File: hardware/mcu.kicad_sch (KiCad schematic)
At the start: 18 parts

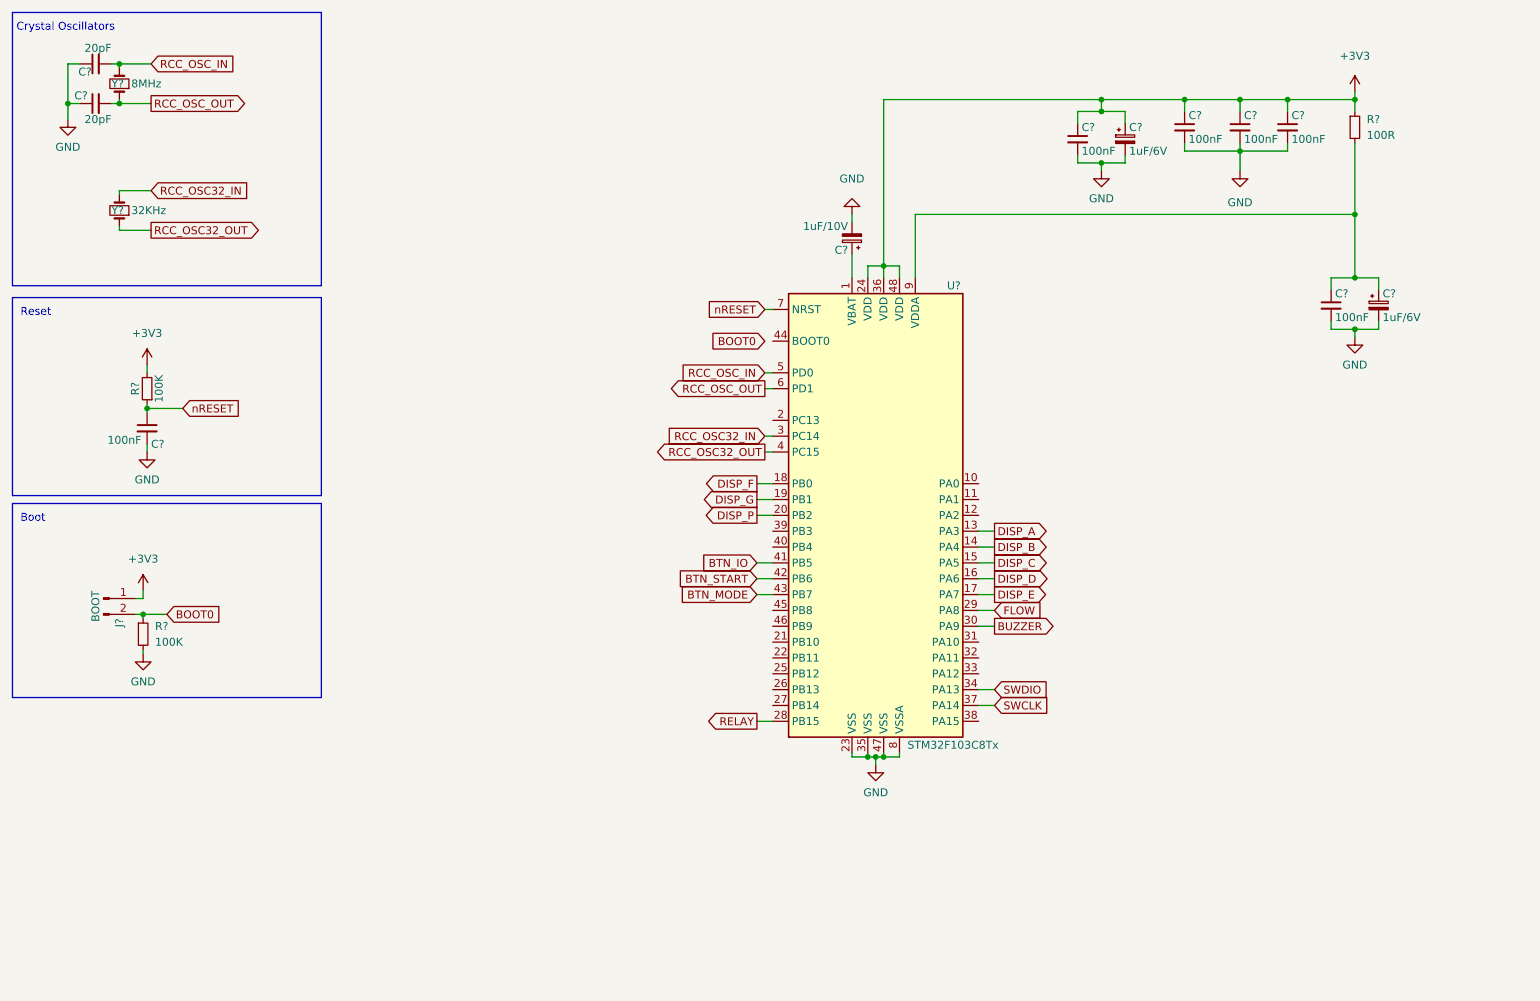
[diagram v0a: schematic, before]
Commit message: Display circuit added
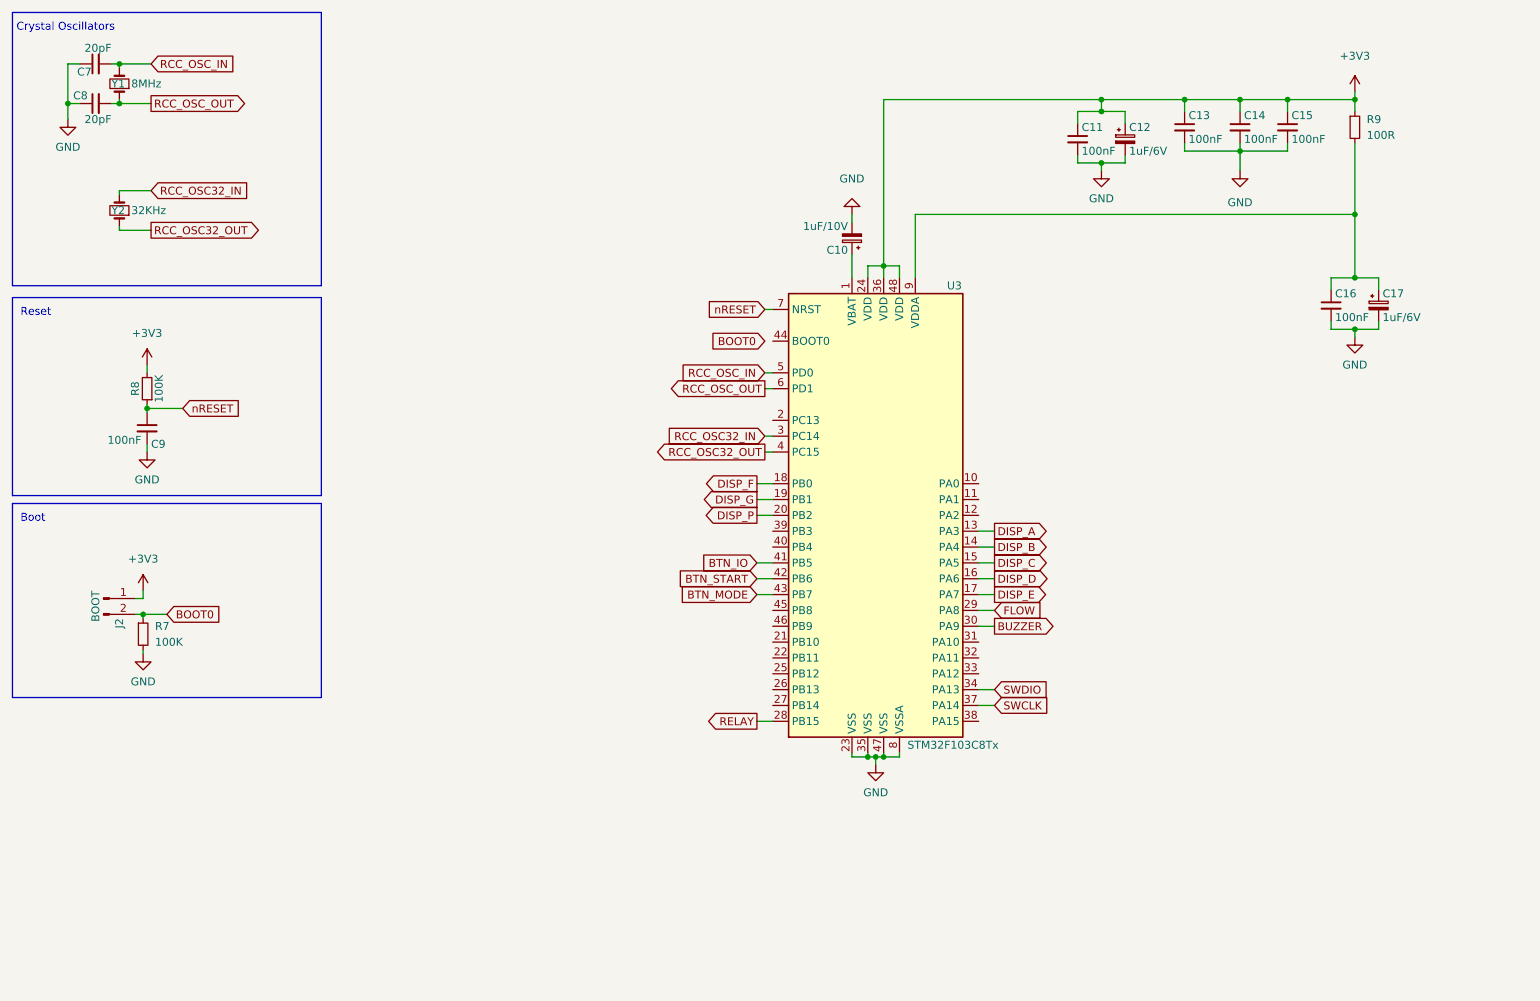
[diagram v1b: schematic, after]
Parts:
- gave numbers to parts that had none: 18
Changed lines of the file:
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@@
   (symbol (lib_id "power:GND") (at 188.595 38.735 0) (unit 1)
     (in_bom yes) (on_board yes) (fields_autoplaced)
-    (property "Reference" "#PWR?" (id 0) (at 188.595 45.085 0)
+    (property "Reference" "#PWR08" (id 0) (at 188.595 45.085 0)
       (effects (font (size 1.27 1.27)) hide)
     )
@@
   (symbol (lib_id "Device:Crystal_Small") (at 31.115 45.085 90) (unit 1)
     (in_bom yes) (on_board yes)
-    (property "Reference" "Y?" (id 0) (at 29.845 45.085 90)
+    (property "Reference" "Y2" (id 0) (at 29.845 45.085 90)
       (effects (font (size 1.27 1.27)) (justify right))
     )
@@
   (symbol (lib_id "Device:C_Small") (at 210.82 31.75 0) (unit 1)
     (in_bom yes) (on_board yes)
-    (property "Reference" "C?" (id 0) (at 211.455 29.845 0)
+    (property "Reference" "C14" (id 0) (at 211.455 29.845 0)
       (effects (font (size 1.27 1.27)) (justify left))
     )
@@
   (symbol (lib_id "power:+3V3") (at 35.56 69.85 0) (unit 1)
     (in_bom yes) (on_board yes) (fields_autoplaced)
-    (property "Reference" "#PWR?" (id 0) (at 35.56 73.66 0)
+    (property "Reference" "#PWR04" (id 0) (at 35.56 73.66 0)
       (effects (font (size 1.27 1.27)) hide)
     )
@@
   (symbol (lib_id "Device:R_Small") (at 35.56 73.66 180) (unit 1)
     (in_bom yes) (on_board yes)
-    (property "Reference" "R?" (id 0) (at 33.655 73.66 90))
+    (property "Reference" "R8" (id 0) (at 33.655 73.66 90))
     (property "Value" "100K" (id 1) (at 37.465 73.66 90))
     (property "Footprint" "" (id 2) (at 35.56 73.66 0)
@@
   (symbol (lib_id "Device:C_Polarized_Small") (at 148.59 49.53 180) (unit 1)
     (in_bom yes) (on_board yes)
-    (property "Reference" "C?" (id 0) (at 147.955 51.435 0)
+    (property "Reference" "C10" (id 0) (at 147.955 51.435 0)
       (effects (font (size 1.27 1.27)) (justify left))
     )
@@
   (symbol (lib_id "power:GND") (at 148.59 45.72 180) (unit 1)
     (in_bom yes) (on_board yes) (fields_autoplaced)
-    (property "Reference" "#PWR?" (id 0) (at 148.59 39.37 0)
+    (property "Reference" "#PWR06" (id 0) (at 148.59 39.37 0)
       (effects (font (size 1.27 1.27)) hide)
     )
@@
   (symbol (lib_id "Device:C_Polarized_Small") (at 192.405 33.655 0) (unit 1)
     (in_bom yes) (on_board yes)
-    (property "Reference" "C?" (id 0) (at 193.04 31.75 0)
+    (property "Reference" "C12" (id 0) (at 193.04 31.75 0)
       (effects (font (size 1.27 1.27)) (justify left))
     )
@@
   (symbol (lib_id "Device:C_Small") (at 184.785 33.655 0) (unit 1)
     (in_bom yes) (on_board yes)
-    (property "Reference" "C?" (id 0) (at 185.42 31.75 0)
+    (property "Reference" "C11" (id 0) (at 185.42 31.75 0)
       (effects (font (size 1.27 1.27)) (justify left))
     )
@@
   (symbol (lib_id "power:+3V3") (at 229.235 26.035 0) (unit 1)
     (in_bom yes) (on_board yes) (fields_autoplaced)
-    (property "Reference" "#PWR?" (id 0) (at 229.235 29.845 0)
+    (property "Reference" "#PWR010" (id 0) (at 229.235 29.845 0)
       (effects (font (size 1.27 1.27)) hide)
     )
@@
   (symbol (lib_id "power:GND") (at 35.56 83.82 0) (unit 1)
     (in_bom yes) (on_board yes) (fields_autoplaced)
-    (property "Reference" "#PWR?" (id 0) (at 35.56 90.17 0)
+    (property "Reference" "#PWR05" (id 0) (at 35.56 90.17 0)
       (effects (font (size 1.27 1.27)) hide)
     )
@@
   (symbol (lib_id "power:GND") (at 229.235 65.405 0) (unit 1)
     (in_bom yes) (on_board yes) (fields_autoplaced)
-    (property "Reference" "#PWR?" (id 0) (at 229.235 71.755 0)
+    (property "Reference" "#PWR019" (id 0) (at 229.235 71.755 0)
       (effects (font (size 1.27 1.27)) hide)
     )
@@
   (symbol (lib_id "Device:R_Small") (at 34.925 113.03 0) (unit 1)
     (in_bom yes) (on_board yes) (fields_autoplaced)
-    (property "Reference" "R?" (id 0) (at 36.83 111.7599 0)
+    (property "Reference" "R7" (id 0) (at 36.83 111.7599 0)
       (effects (font (size 1.27 1.27)) (justify left))
     )
@@
   (symbol (lib_id "Device:R_Small") (at 229.235 31.75 0) (unit 1)
     (in_bom yes) (on_board yes) (fields_autoplaced)
-    (property "Reference" "R?" (id 0) (at 231.14 30.4799 0)
+    (property "Reference" "R9" (id 0) (at 231.14 30.4799 0)
       (effects (font (size 1.27 1.27)) (justify left))
     )
@@
   (symbol (lib_id "Device:C_Small") (at 27.305 21.59 90) (unit 1)
     (in_bom yes) (on_board yes)
-    (property "Reference" "C?" (id 0) (at 26.67 22.86 90)
+    (property "Reference" "C7" (id 0) (at 26.67 22.86 90)
       (effects (font (size 1.27 1.27)) (justify left))
     )
@@
   (symbol (lib_id "Device:C_Small") (at 201.93 31.75 0) (unit 1)
     (in_bom yes) (on_board yes)
-    (property "Reference" "C?" (id 0) (at 202.565 29.845 0)
+    (property "Reference" "C13" (id 0) (at 202.565 29.845 0)
       (effects (font (size 1.27 1.27)) (justify left))
     )
@@
   (symbol (lib_id "Device:C_Polarized_Small") (at 233.045 60.325 0) (unit 1)
     (in_bom yes) (on_board yes)
-    (property "Reference" "C?" (id 0) (at 233.68 58.42 0)
+    (property "Reference" "C17" (id 0) (at 233.68 58.42 0)
       (effects (font (size 1.27 1.27)) (justify left))
     )
@@
   (symbol (lib_id "power:GND") (at 152.4 133.985 0) (unit 1)
     (in_bom yes) (on_board yes) (fields_autoplaced)
-    (property "Reference" "#PWR?" (id 0) (at 152.4 140.335 0)
+    (property "Reference" "#PWR07" (id 0) (at 152.4 140.335 0)
       (effects (font (size 1.27 1.27)) hide)
     )
@@
   (symbol (lib_id "Device:C_Small") (at 225.425 60.325 0) (unit 1)
     (in_bom yes) (on_board yes)
-    (property "Reference" "C?" (id 0) (at 226.06 58.42 0)
+    (property "Reference" "C16" (id 0) (at 226.06 58.42 0)
       (effects (font (size 1.27 1.27)) (justify left))
     )
@@
   (symbol (lib_id "Device:C_Small") (at 27.305 27.94 90) (unit 1)
     (in_bom yes) (on_board yes)
-    (property "Reference" "C?" (id 0) (at 26.035 26.67 90)
+    (property "Reference" "C8" (id 0) (at 26.035 26.67 90)
       (effects (font (size 1.27 1.27)) (justify left))
     )
@@
   (symbol (lib_id "Device:C_Small") (at 218.44 31.75 0) (unit 1)
     (in_bom yes) (on_board yes)
-    (property "Reference" "C?" (id 0) (at 219.075 29.845 0)
+    (property "Reference" "C15" (id 0) (at 219.075 29.845 0)
       (effects (font (size 1.27 1.27)) (justify left))
     )
@@
   (symbol (lib_id "power:GND") (at 22.86 30.48 0) (unit 1)
     (in_bom yes) (on_board yes) (fields_autoplaced)
-    (property "Reference" "#PWR?" (id 0) (at 22.86 36.83 0)
+    (property "Reference" "#PWR01" (id 0) (at 22.86 36.83 0)
       (effects (font (size 1.27 1.27)) hide)
     )
@@
   (symbol (lib_id "Connector:Conn_01x02_Male") (at 28.575 107.315 0) (unit 1)
     (in_bom yes) (on_board yes)
-    (property "Reference" "J?" (id 0) (at 31.115 110.49 90)
+    (property "Reference" "J2" (id 0) (at 31.115 110.49 90)
       (effects (font (size 1.27 1.27)) (justify right))
     )
@@
   (symbol (lib_id "power:GND") (at 34.925 116.205 0) (unit 1)
     (in_bom yes) (on_board yes) (fields_autoplaced)
-    (property "Reference" "#PWR?" (id 0) (at 34.925 122.555 0)
+    (property "Reference" "#PWR03" (id 0) (at 34.925 122.555 0)
       (effects (font (size 1.27 1.27)) hide)
     )
@@
   (symbol (lib_id "Device:C_Small") (at 35.56 80.01 0) (unit 1)
     (in_bom yes) (on_board yes)
-    (property "Reference" "C?" (id 0) (at 36.195 82.55 0)
+    (property "Reference" "C9" (id 0) (at 36.195 82.55 0)
       (effects (font (size 1.27 1.27)) (justify left))
     )
@@
   (symbol (lib_id "Device:Crystal_Small") (at 31.115 24.765 90) (unit 1)
     (in_bom yes) (on_board yes)
-    (property "Reference" "Y?" (id 0) (at 29.845 24.765 90)
+    (property "Reference" "Y1" (id 0) (at 29.845 24.765 90)
       (effects (font (size 1.27 1.27)) (justify right))
     )
@@
   (symbol (lib_id "power:GND") (at 210.82 38.735 0) (unit 1)
     (in_bom yes) (on_board yes) (fields_autoplaced)
-    (property "Reference" "#PWR?" (id 0) (at 210.82 45.085 0)
+    (property "Reference" "#PWR09" (id 0) (at 210.82 45.085 0)
       (effects (font (size 1.27 1.27)) hide)
     )
@@
   (symbol (lib_id "power:+3V3") (at 34.925 106.045 0) (unit 1)
     (in_bom yes) (on_board yes) (fields_autoplaced)
-    (property "Reference" "#PWR?" (id 0) (at 34.925 109.855 0)
+    (property "Reference" "#PWR02" (id 0) (at 34.925 109.855 0)
       (effects (font (size 1.27 1.27)) hide)
     )
@@
   (symbol (lib_id "MCU_ST_STM32F1:STM32F103C8Tx") (at 153.67 93.98 0) (unit 1)
     (in_bom yes) (on_board yes)
-    (property "Reference" "U?" (id 0) (at 163.83 57.15 0)
-      (effects (font (size 1.27 1.27)) (justify left))
-    )
+    (property "Reference" "U3" (id 0) (at 163.83 57.15 0)
+      (effects (font (size 1.27 1.27)) (justify left))
+    )

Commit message: Schematics are completed
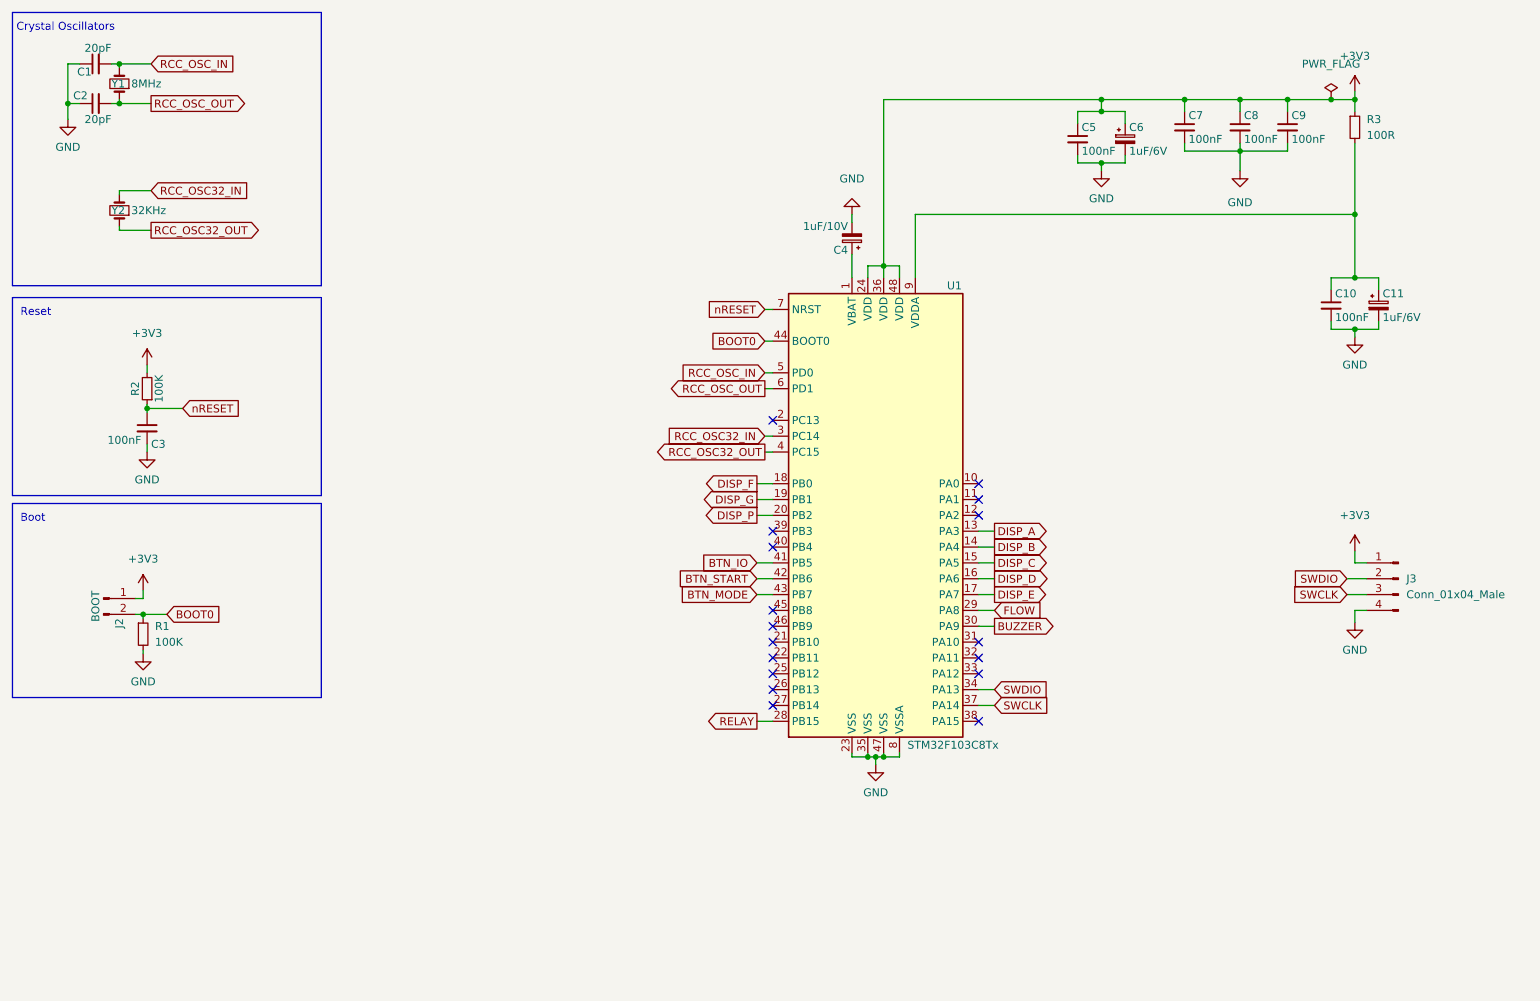
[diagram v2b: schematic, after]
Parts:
- added J3: Conn_01x04_Male, Connector_PinHeader_2.54mm:PinHeader_1x04_P2.54mm_Vertical, symbol Connector:Conn_01x04_Male
- C1: renamed from C7; footprint (none) -> Capacitor_SMD:C_0603_1608Metric
- C10: renamed from C16; footprint (none) -> Capacitor_SMD:C_0603_1608Metric
- C11: renamed from C17; footprint (none) -> Capacitor_SMD:CP_Elec_6.3x7.7
- C2: renamed from C8; footprint (none) -> Capacitor_SMD:C_0603_1608Metric
- C3: renamed from C9; footprint (none) -> Capacitor_SMD:C_0603_1608Metric
- C4: renamed from C10; footprint (none) -> Capacitor_SMD:CP_Elec_6.3x7.7
- C5: renamed from C11; footprint (none) -> Capacitor_SMD:C_0603_1608Metric
- C6: renamed from C12; footprint (none) -> Capacitor_SMD:CP_Elec_6.3x7.7
- C7: renamed from C13; footprint (none) -> Capacitor_SMD:C_0603_1608Metric
- C8: renamed from C14; footprint (none) -> Capacitor_SMD:C_0603_1608Metric
- C9: renamed from C15; footprint (none) -> Capacitor_SMD:C_0603_1608Metric
- J2: footprint (none) -> Connector_PinHeader_2.54mm:PinHeader_1x02_P2.54mm_Vertical
- R1: renamed from R7; footprint (none) -> Resistor_SMD:R_0603_1608Metric
- R2: renamed from R8; footprint (none) -> Resistor_SMD:R_0603_1608Metric
- R3: renamed from R9; footprint (none) -> Resistor_SMD:R_0603_1608Metric
- Y1: footprint (none) -> Crystal:Crystal_SMD_HC49-SD
- Y2: footprint (none) -> Crystal:Crystal_C38-LF_D3.0mm_L8.0mm_Vertical
- renumbered U3 to U1
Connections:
- net +3V3: now also J3.1 (Pin_1)
- net BOOT0: now also U1.44 (BOOT0)
- net GND: now also J3.4 (Pin_4)
- net SWCLK: now also J3.3 (Pin_3)
- net SWDIO: now also J3.2 (Pin_2)
- no-connect marks 0 -> 17
